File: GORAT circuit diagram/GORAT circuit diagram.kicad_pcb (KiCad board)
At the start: 2 copper layers, 56 x 56 mm, 51 parts, among them J1 AudioJack2, J2 AudioJack2, J3 Barrel_Jack_PTH_Slot, J4 Conn_01x09_Socket, J5 Conn_01x09_Socket, SW3 SW_Rotary4x3, U1 LM308N

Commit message: asdsa
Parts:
- added C18: 470n, Capacitor_THT:C_Disc_D4.7mm_W2.5mm_P5.00mm, F.Cu at (47.6, 49.1)
- added C19: 1u, Capacitor_THT:CP_Radial_D5.0mm_P2.50mm, F.Cu at (56.3, 50.4)
- added R15: 22k, Resistor_THT:R_Axial_DIN0207_L6.3mm_D2.5mm_P10.16mm_Horizontal, F.Cu at (70.8, 37.4)
- added R16: 22k, Resistor_THT:R_Axial_DIN0207_L6.3mm_D2.5mm_P10.16mm_Horizontal, F.Cu at (70.8, 41.4)
- added R17: 22k, Resistor_THT:R_Axial_DIN0207_L6.3mm_D2.5mm_P10.16mm_Horizontal, F.Cu at (70.8, 45.5)
- added R18: 1M, Resistor_THT:R_Axial_DIN0207_L6.3mm_D2.5mm_P10.16mm_Horizontal, F.Cu at (70.8, 49.5)
- added RV4-BLEND1: 100K, Connector_Wire:SolderWire-0.75sqmm_1x06_P7mm_D1.25mm_OD3.5mm, F.Cu at (179.5, 88.0)
- added U2: TL072ACP, PCM_Package_DIP_AKL:DIP-8_W7.62mm_LongPads, F.Cu at (48.0, 37.4)
- added U3: TL072ACP, PCM_Package_DIP_AKL:DIP-8_W7.62mm_LongPads, F.Cu at (59.6, 37.4)
- moved R13 64.6 mm to (178.0, 112.5), turned to 180 degrees
- moved D4 58.9 mm to (177.0, 124.0)
- moved J5 56.8 mm to (158.8, 108.0)
- moved S1 56.6 mm to (163.5, 124.0)
- moved J2 51.7 mm to (122.0, 54.0)
- moved J1 51.6 mm to (163.5, 53.5)
- moved SW3 49.6 mm to (121.4, 116.4)
- moved RV2-FILTER1 46.8 mm to (127.5, 71.5)
- moved RV1-GAIN1 44.5 mm to (113.0, 78.0)
- moved RV3-VOL1 38.3 mm to (147.5, 71.5)
- moved J4 27.1 mm to (156.8, 92.5)
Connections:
- C1 pad 2: Net-(C1-Pad2) -> Net-(U2A-+)
- R2 pad 1: Net-(C1-Pad2) -> Net-(U2A-+)
- R3 pad 2: Net-(C1-Pad2) -> Net-(U2A--)
- RV3-VOL1 pad 2: SigOut -> SigRAT
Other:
- board outline removed

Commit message: almost done
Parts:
- added J6: Barrel_Jack, Connector_Wire:SolderWire-0.5sqmm_1x02_P4.6mm_D0.9mm_OD2.1mm, F.Cu at (73.0, 69.0)
- added J7: Conn_01x02_Socket, Connector_PinHeader_2.54mm:PinHeader_1x02_P2.54mm_Vertical, F.Cu at (25.3, 90.5)
- added J8: Conn_01x03_Socket, Connector_PinHeader_2.54mm:PinHeader_1x03_P2.54mm_Vertical, F.Cu at (59.8, 97.0)
- added J9: Conn_01x03_Socket, Connector_PinHeader_2.54mm:PinHeader_1x03_P2.54mm_Vertical, F.Cu at (59.8, 90.5)
- added SW8: SW_Rotary2x6, Daves customs:RS26, F.Cu at (62.5, 120.2)
- J3: value Barrel_Jack_PTH_Slot -> Conn_01x08_Socket; footprint PCM_SparkFun-Connector:Barrel_Jack_PTH_Slot -> Connector_PinHeader_2.54mm:PinHeader_1x08_P2.54mm_Vertical
- J4: value Conn_01x09_Socket -> Conn_01x08_Socket; footprint Connector_PinHeader_2.54mm:PinHeader_1x09_P2.54mm_Vertical -> Connector_PinHeader_2.54mm:PinHeader_1x08_P2.54mm_Vertical
- J5: value Conn_01x09_Socket -> Conn_01x02_Socket; footprint Connector_PinHeader_2.54mm:PinHeader_1x09_P2.54mm_Vertical -> Connector_PinHeader_2.54mm:PinHeader_1x02_P2.54mm_Vertical
- RV1-GAIN1, RV2-FILTER1, RV3-VOL1: footprint Connector_Wire:SolderWire-0.75sqmm_1x03_P7mm_D1.25mm_OD3.5mm -> Daves customs:Potentiometer_Alpha_RD901F-40-00D_Single_Vertical
- RV4-BLEND1: footprint Connector_Wire:SolderWire-0.75sqmm_1x06_P7mm_D1.25mm_OD3.5mm -> Potentiometer_THT:Potentiometer_Alpha_RD902F-40-00D_Dual_Vertical
- SW3: footprint Daves customs:Rotary Switch -> Daves customs:RS26
- moved J5 133.9 mm to (25.3, 97.0)
- moved C5 96.0 mm to (29.7, 103.5)
- moved R1 93.3 mm to (108.5, 83.0), turned to 180 degrees
- moved R13 92.8 mm to (85.5, 120.1), turned to 90 degrees
- moved D4 91.3 mm to (85.8, 126.0), turned to 180 degrees
- moved RV1-GAIN1 87.7 mm to (25.3, 78.0), turned to 90 degrees
- moved SW3 86.2 mm to (35.3, 120.2), turned to 75 degrees
- moved R15 83.1 mm to (127.3, 98.3), turned to 180 degrees
- moved U3 81.4 mm to (113.6, 98.3), turned to 180 degrees
- moved R12 79.6 mm to (96.3, 121.1), turned to 90 degrees
- moved C6 79.3 mm to (48.1, 103.5)
- moved J2 78.9 mm to (47.0, 78.5)
- moved R16 77.4 mm to (127.3, 94.3), turned to 180 degrees
- moved R2 76.3 mm to (88.0, 85.9), turned to -90 degrees
- moved R11 72.8 mm to (96.9, 102.5), turned to 180 degrees
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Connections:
- C14 pad 2: GND -> GND3
- C15 pad 2: GND -> GND3
- C16 pad 2: GND -> GND3
- C17 pad 2: GND -> GND3
- C4 pad 2: Net-(U1--) -> Net-(J7-Pin_1)
- C5 pad 2: GND -> GND3
- C6 pad 2: GND -> GND3
- D1 pad 2: GND -> GND3
- D2 pad 1: GND -> GND3
- D4 pad 2: Vin -> Vin1
- D5 pad 2: GND -> GND3
- D6 pad 1: Net-(D6-K) -> GND3
- D6 pad 2: GND -> Net-(D6-A)
- D7 pad 2: GND -> GND3
- D8 pad 1: Net-(D8-K) -> GND3
- D8 pad 2: GND -> Net-(D8-A)
- J1 pad 1: /JackIn -> /JackIn1
- J2 pad 1: /JackOut -> /JackOut1
- J4 pad 1: Bypass -> Bypass2
- J4 pad 2: /JackIn -> /JackIn2
- J4 pad 3: /JackOut -> /JackOut2
- J4 pad 4: SigIn -> SigIn2
- J4 pad 5: SigOut -> SigOut2
- J4 pad 6: /+9v Jack -> /+9v Jack2
- J4 pad 7: Vin -> Vin2
- J4 pad 8: GND -> GND2
- J5 pad 1: Bypass -> Net-(J5-Pin_1)
- J5 pad 2: /JackIn -> GND3
- R1 pad 2: /JackIn -> /JackIn1
- R10 pad 1: Vin -> Vin1
- R14 pad 2: /JackOut -> /JackOut1
- R4 pad 1: Net-(U1--) -> Net-(J5-Pin_1)
- R5 pad 1: Net-(U1--) -> Net-(J5-Pin_1)
- R6 pad 1: Net-(R6-Pad1) -> Net-(J9-Pin_1)
- RV1-GAIN1 pad 1: Net-(U1--) -> Net-(J7-Pin_1)
- RV1-GAIN1 pad 2: Net-(U1--) -> Net-(J7-Pin_1)
- RV2-FILTER1 pad 1: Net-(R6-Pad1) -> Net-(J9-Pin_1)
- RV2-FILTER1 pad 2: Net-(R6-Pad1) -> Net-(R7-Pad2)
- RV3-VOL1 pad 1: Net-(C10-Pad2) -> GND
- RV3-VOL1 pad 3: GND -> Net-(C10-Pad2)
- RV4-BLEND1 pad 5: SigDRY -> Net-(R17-Pad1)
- S1 pad P$1: SigOut -> SigOut2
- S1 pad P$2: /JackOut -> /JackOut2
- S1 pad P$3: Bypass -> Net-(S1A-S)
- S1 pad P$4: SigIn -> SigIn2
- S1 pad P$5: /JackIn -> /JackIn2
- S1 pad P$6: Bypass -> Net-(S1A-S)
- S1 pad P$7: /+9v Jack -> /+9v Jack2
- S1 pad P$8: Vin -> Vin2
- U1 pad 2: Net-(U1--) -> Net-(J7-Pin_1)
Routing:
- net GND: track 0.00 -> 217.3 mm
- net +9V: track 0.00 -> 113.1 mm
- net GND3: track 0.00 -> 111.3 mm
- net /JackOut1: track 0.00 -> 92.3 mm, vias 0 -> 1
- net /+9v Jack1: track 0.00 -> 77.1 mm, vias 0 -> 1
- net Net-(J7-Pin_1): track 0.00 -> 72.9 mm
- net Net-(C4-Pad1): track 0.00 -> 60.9 mm
- net +4.5V: track 0.00 -> 58.9 mm
- net Vin1: track 0.00 -> 53.4 mm
- net Net-(D7-K): track 0.00 -> 50.4 mm
- net Net-(C9-Pad1): track 0.00 -> 45.5 mm, vias 0 -> 1
- net /JackIn1: track 0.00 -> 43.3 mm
- net Net-(R4-Pad2): track 0.00 -> 42.5 mm, vias 0 -> 1
- net Net-(J9-Pin_1): track 0.00 -> 41.1 mm
- net SigRAT: track 0.00 -> 36.4 mm
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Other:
- board outline added: 107.5 x 71.5 mm

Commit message: close to done
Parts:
- removed JN1: 2N5458, 2N5458:TO92
- added C20: 220n, Capacitor_THT:C_Disc_D5.1mm_W3.2mm_P5.00mm, F.Cu at (35.5, 100.5)
- added C21: 470n, Capacitor_THT:C_Disc_D5.1mm_W3.2mm_P5.00mm, F.Cu at (51.0, 109.5)
- added C22: 33p, Capacitor_THT:C_Disc_D4.7mm_W2.5mm_P5.00mm, F.Cu at (57.5, 106.0)
- added J10: Conn_01x02_Socket, Connector_PinHeader_2.54mm:PinHeader_1x02_P2.54mm_Vertical, F.Cu at (33.2, 90.5)
- added J11: Conn_01x02_Socket, Connector_PinHeader_2.54mm:PinHeader_1x02_P2.54mm_Vertical, F.Cu at (33.5, 97.0)
- added Q1: J111, PCM_Package_TO_SOT_THT_AKL:TO-92_Inline_Wide_DSG, F.Cu at (65.5, 83.6)
- C16: value Xu -> 68p; footprint Capacitor_THT:CP_Radial_D5.0mm_P2.50mm -> Capacitor_THT:C_Disc_D4.7mm_W2.5mm_P5.00mm
- C17: value Xu -> 47p; footprint Capacitor_THT:CP_Radial_D5.0mm_P2.50mm -> Capacitor_THT:C_Disc_D4.7mm_W2.5mm_P5.00mm
- U1: value LM308N -> OP07CP
- moved C16 18.4 mm to (54.0, 106.0), turned to 90 degrees
- moved D1 13.5 mm to (72.5, 108.0)
- moved R5 7.45 mm to (39.3, 96.0)
- moved C17 7.16 mm to (61.0, 106.0), turned to 90 degrees
- moved R4 6.57 mm to (39.4, 99.5)
- moved D8 5.52 mm to (77.5, 112.2)
- moved D2 3.74 mm to (79.8, 105.0)
- moved C6 2.10 mm to (47.5, 105.5), turned to 90 degrees
- moved C15 1.71 mm to (42.0, 105.2), turned to 90 degrees
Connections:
- C16 pad 2: GND3 -> Net-(J11-Pin_2)
- C17 pad 2: GND3 -> Net-(J11-Pin_2)
- SW3 pad 15: unconnected-(SW3-Pad15) -> Net-(J11-Pin_1)
- SW3 pad 3: Net-(C16-Pad1) -> Net-(C20-Pad2)
- SW3 pad 6: Net-(C17-Pad1) -> Net-(C21-Pad2)
- SW3 pad 7: unconnected-(SW3-Pad7) -> Net-(C16-Pad1)
- SW3 pad 8: unconnected-(SW3-Pad8) -> Net-(C17-Pad1)
- SW3 pad 9: unconnected-(SW3-Pad9) -> Net-(C22-Pad1)
- U1 pad 1: Net-(C3-Pad1) -> Net-(J10-Pin_2)
- U1 pad 8: Net-(C3-Pad2) -> Net-(J10-Pin_1)
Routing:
- net Net-(J10-Pin_1): track 0.00 -> 47.4 mm
- net Net-(J10-Pin_2): track 0.00 -> 44.3 mm, vias 0 -> 1
- net Net-(C22-Pad1): track 0.00 -> 34.6 mm
- net Net-(J11-Pin_1): track 0.00 -> 29.6 mm
- net Net-(J11-Pin_2): track 0.00 -> 26.7 mm
- net Net-(C17-Pad1): track 17.2 -> 31.2 mm
- net Net-(C16-Pad1): track 7.33 -> 20.3 mm
- net /+9v Jack1: track 77.1 -> 65.8 mm
- net Net-(R4-Pad2): track 42.5 -> 31.9 mm
- net Net-(C21-Pad2): track 0.00 -> 7.79 mm
- net Net-(D1-K): track 27.7 -> 33.7 mm
- net Net-(C20-Pad2): track 0.00 -> 5.20 mm
- net Net-(D7-K): track 50.4 -> 45.4 mm
- net Net-(J5-Pin_1): track 22.5 -> 18.3 mm
- net Net-(D2-A): track 19.8 -> 16.4 mm
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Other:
- board size 107.5 x 71.5 mm -> 108.5 x 71.5 mm
- board text added: "+9V"
- board text added: "Board 1 : The meat and potatoes"
- board text added: "Board 2 : Tone Selekta"
- board text added: "Board 3 : Stompy"
- board text added: "GND"
- board text added: "Output"

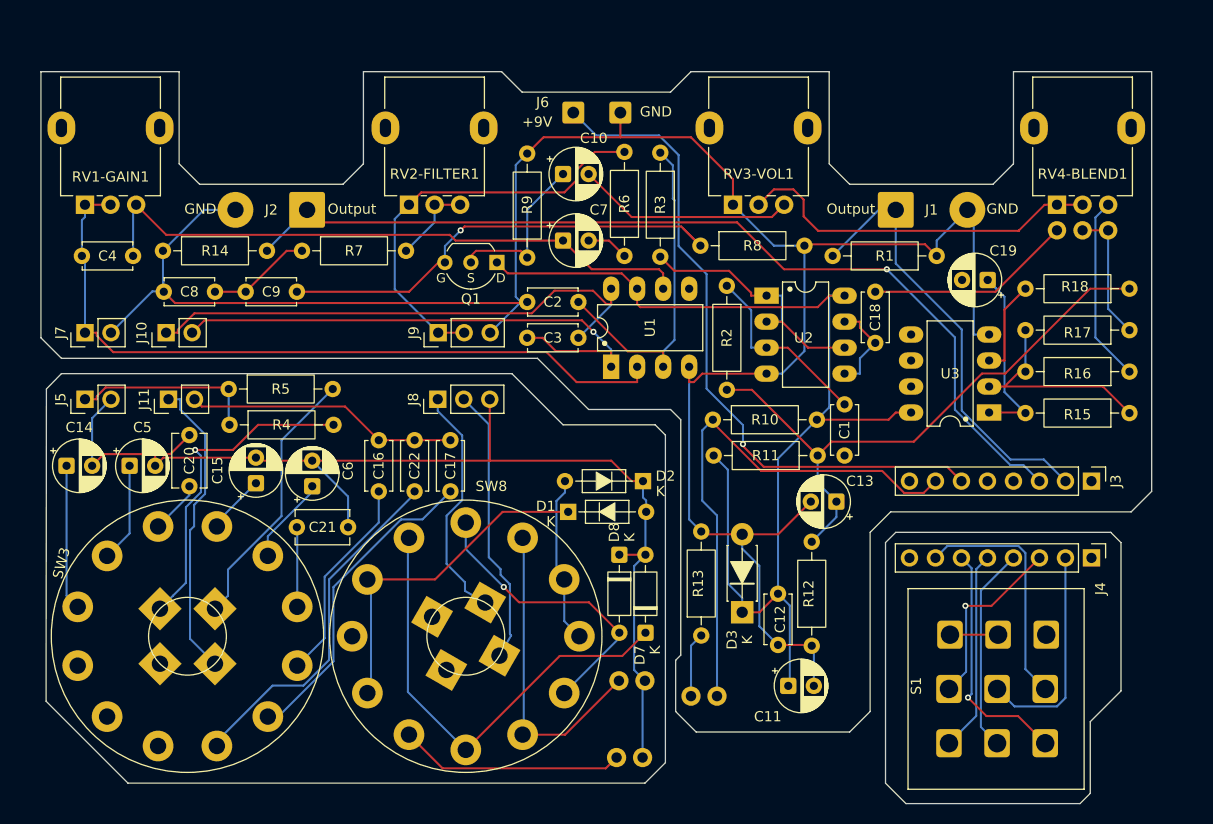
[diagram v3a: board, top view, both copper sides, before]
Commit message: Update KiCad PCB, add backups and artwork
Modify GORAT circuit diagram.kicad_pcb: reorder/renumber nets, adjust several pad/net assignments and component positions, and add numerous F.Fab properties (Availability, Check_prices, Description_1, MF, MP, Package, Price, Sim.Type, SnapEDA_Link) for multiple footprints. Remove several old backup ZIPs and add new timestamped backup ZIPs. Add new project assets: GoRAT.csv and artwork/renders (goram-mirror.svg, goram.png, goram.svg, underside.svg). These changes appear to be from a PCB/footprint update and exporting backup/artwork files.
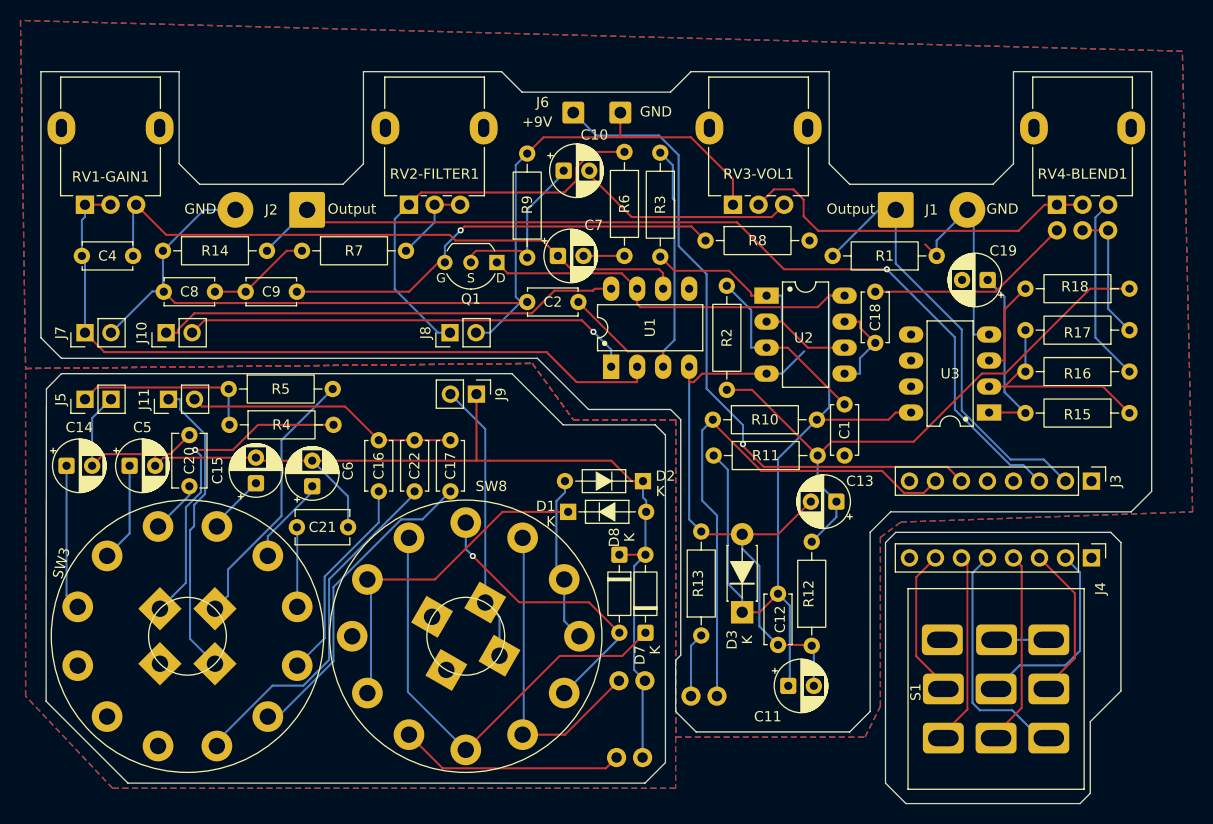
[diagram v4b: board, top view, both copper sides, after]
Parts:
- removed C3: 30p, Capacitor_THT:C_Disc_D4.7mm_W2.5mm_P5.00mm
- J8, J9: value Conn_01x03_Socket -> Conn_01x02_Socket; footprint Connector_PinHeader_2.54mm:PinHeader_1x03_P2.54mm_Vertical -> Connector_PinHeader_2.54mm:PinHeader_1x02_P2.54mm_Vertical
- moved J9 7.07 mm to (63.5, 96.5), turned to -90 degrees
- moved J8 6.61 mm to (61.0, 90.5)
- moved C7 1.58 mm to (71.5, 83.0)
- moved R8 0.71 mm to (85.9, 81.5)
- moved C10 0.33 mm to (72.1, 74.7)
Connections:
- net Net-(S1A-S) renamed /Bypass
- J8 pad 2: Net-(J8-Pin_2) -> GND
- J9 pad 1: Net-(J9-Pin_1) -> GND3
- J9 pad 2: Net-(J9-Pin_1) -> Net-(J9-Pin_2)
- R6 pad 1: Net-(J9-Pin_1) -> Net-(J8-Pin_1)
- RV2-FILTER1 pad 1: Net-(J9-Pin_1) -> Net-(J8-Pin_1)
- SW8 pad 13: Net-(J8-Pin_1) -> Net-(J9-Pin_2)
- SW8 pad 14: Net-(J8-Pin_2) -> Net-(J9-Pin_2)
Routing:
- net Net-(J9-Pin_1): track 41.1 -> 0.00 mm
- net GND: track 218.6 -> 189.4 mm
- net Net-(J9-Pin_2): track 0.00 -> 27.5 mm
- net Net-(J8-Pin_2): track 27.3 -> 0.00 mm
- net Net-(J8-Pin_1): track 23.4 -> 39.9 mm
- net Net-(C3-Pad1): track 10.2 -> 0.00 mm
- net Vin2: track 23.6 -> 14.2 mm
- net Net-(C3-Pad2): track 6.12 -> 0.00 mm
- net /+9v Jack2: track 23.6 -> 18.3 mm, vias 1 -> 0
- net SigOut2: track 19.7 -> 23.5 mm
- net /JackOut2: track 18.0 -> 14.8 mm, vias 1 -> 0
- net Net-(Q1-G): track 46.1 -> 44.1 mm
- net /JackIn2: track 21.4 -> 19.4 mm
- net Net-(J10-Pin_1): track 47.4 -> 45.4 mm
- net SigIn2: track 20.1 -> 18.4 mm
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- added copper zone on B.Cu, net GND
- added copper zone on F.Cu, net GND
- added copper zone on B.Cu, net GND3
- added copper zone on F.Cu, net GND3
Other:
- board text added: "GoRAT Distortion Effect V1.1 RandomAccessCrew"

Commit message: Update disc capacitor footprints and BOM
Replace THT disc capacitor footprints with smaller C_Disc_D4.7mm_W2.5mm variants across schematic and PCB (updated 3D model paths, silk/text positions, rotations and UUIDs). Update project metadata: change active board layer in .kicad_prl, set BOM export filename in .kicad_pro, and add generated BOM CSV/XLSX. Add KiCad backup archives and remove autosave/.lck temporary files to keep the repo clean.
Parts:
- C20, C21: footprint Capacitor_THT:C_Disc_D5.1mm_W3.2mm_P5.00mm -> Capacitor_THT:C_Disc_D4.7mm_W2.5mm_P5.00mm
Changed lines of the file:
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@@
 		)
 	)
-	(footprint "Capacitor_THT:C_Disc_D5.1mm_W3.2mm_P5.00mm"
+	(footprint "Capacitor_THT:C_Disc_D4.7mm_W2.5mm_P5.00mm"
 		(layer "F.Cu")
 		(at 51 109.5 180)
-		(descr "C, Disc series, Radial, pin pitch=5.00mm, diameter*width=5.1*3.2mm^2, Capacitor, http://www.vishay.com/docs/45233/krseries.pdf")
-		(tags "C Disc series Radial pin pitch 5.00mm diameter 5.1mm width 3.2mm Capacitor")
+		(descr "C, Disc series, Radial, pin pitch=5.00mm, diameter*width=4.7*2.5mm^2, Capacitor, http://www.vishay.com/docs/45233/krseries.pdf")
+		(tags "C Disc series Radial pin pitch 5.00mm diameter 4.7mm width 2.5mm Capacitor")
 		(property "Reference" "C21"
-			(at 2.5 0 0)
+			(at 2.5 -2.5 180)
 			(layer "F.SilkS")
 			(effects
@@
 		)
 		(property "Value" "470n"
-			(at 2.5 2.85 0)
+			(at 2.5 2.5 180)
 			(layer "F.Fab")
 			(effects
@@
 		)
 		(property "Datasheet" "~"
-			(at 0 0 0)
+			(at 0 0 180)
 			(layer "F.Fab")
 			(hide yes)
@@
 		)
 		(property "Description" "Unpolarized capacitor"
-			(at 0 0 0)
+			(at 0 0 180)
 			(layer "F.Fab")
 			(hide yes)
@@
 		(attr through_hole)
 		(fp_line
-			(start 5.17 1.72)
-			(end -0.17 1.72)
+			(start 4.97 1.37)
+			(end 0.03 1.37)
 			(stroke
 				(width 0.12)
@@
 		)
 		(fp_line
-			(start 5.17 1.026)
-			(end 5.17 1.72)
+			(start 4.97 1.04)
+			(end 4.97 1.37)
 			(stroke
 				(width 0.12)
@@
 		)
 		(fp_line
-			(start 5.17 -1.72)
-			(end 5.17 -1.026)
+			(start 4.97 -1.37)
+			(end 4.97 -1.04)
 			(stroke
 				(width 0.12)
@@
 		)
 		(fp_line
-			(start -0.17 1.72)
-			(end -0.17 1.026)
+			(start 0.03 1.37)
+			(end 0.03 1.04)
 			(stroke
 				(width 0.12)
@@
 		)
 		(fp_line
-			(start -0.17 -1.026)
-			(end -0.17 -1.72)
+			(start 0.03 -1.04)
+			(end 0.03 -1.37)
 			(stroke
 				(width 0.12)
@@
 		)
 		(fp_line
-			(start -0.17 -1.72)
-			(end 5.17 -1.72)
+			(start 0.03 -1.37)
+			(end 4.97 -1.37)
 			(stroke
 				(width 0.12)
@@
 		)
 		(fp_rect
-			(start -1.05 -1.85)
-			(end 6.05 1.85)
+			(start -1.05 -1.5)
+			(end 6.05 1.5)
 			(stroke
 				(width 0.05)
@@
 		)
 		(fp_rect
-			(start -0.05 -1.6)
-			(end 5.05 1.6)
+			(start 0.15 -1.25)
+			(end 4.85 1.25)
 			(stroke
 				(width 0.1)
@@
 		)
 		(fp_text user "${REFERENCE}"
-			(at 2.5 0 0)
+			(at 2.5 0 180)
 			(layer "F.Fab")
 			(effects
 				(font
-					(size 1 1)
-					(thickness 0.15)
+					(size 0.94 0.94)
+					(thickness 0.141)
 				)
 			)
@@
 		)
 		(embedded_fonts no)
-		(model "${KICAD9_3DMODEL_DIR}/Capacitor_THT.3dshapes/C_Disc_D5.1mm_W3.2mm_P5.00mm.step"
+		(model "${KICAD9_3DMODEL_DIR}/Capacitor_THT.3dshapes/C_Disc_D4.7mm_W2.5mm_P5.00mm.step"
 			(offset
 				(xyz 0 0 0)
@@
 		)
 	)
-	(footprint "Capacitor_THT:C_Disc_D5.1mm_W3.2mm_P5.00mm"
+	(footprint "Capacitor_THT:C_Disc_D4.7mm_W2.5mm_P5.00mm"
 		(layer "F.Cu")
 		(at 35.5 100.5 -90)
-		(descr "C, Disc series, Radial, pin pitch=5.00mm, diameter*width=5.1*3.2mm^2, Capacitor, http://www.vishay.com/docs/45233/krseries.pdf")
-		(tags "C Disc series Radial pin pitch 5.00mm diameter 5.1mm width 3.2mm Capacitor")
+		(descr "C, Disc series, Radial, pin pitch=5.00mm, diameter*width=4.7*2.5mm^2, Capacitor, http://www.vishay.com/docs/45233/krseries.pdf")
+		(tags "C Disc series Radial pin pitch 5.00mm diameter 4.7mm width 2.5mm Capacitor")
 		(property "Reference" "C20"
-			(at 2.5 0 90)
+			(at 2.5 0 270)
 			(layer "F.SilkS")
 			(effects
@@
 		)
 		(property "Value" "220n"
-			(at 2.5 2.85 90)
+			(at 2.5 2.5 270)
 			(layer "F.Fab")
 			(effects
@@
 		)
 		(property "Datasheet" "~"
-			(at 0 0 90)
+			(at 0 0 270)
 			(layer "F.Fab")
 			(hide yes)
@@
 		)
 		(property "Description" "Unpolarized capacitor"
-			(at 0 0 90)
+			(at 0 0 270)
 			(layer "F.Fab")
 			(hide yes)
@@
 		(attr through_hole)
 		(fp_line
-			(start -0.17 1.72)
-			(end -0.17 1.026)
+			(start 0.03 1.37)
+			(end 0.03 1.04)
 			(stroke
 				(width 0.12)
@@
 		)
 		(fp_line
-			(start 5.17 1.72)
-			(end -0.17 1.72)
+			(start 4.97 1.37)
+			(end 0.03 1.37)
 			(stroke
 				(width 0.12)
@@
 		)
 		(fp_line
-			(start 5.17 1.026)
-			(end 5.17 1.72)
+			(start 4.97 1.04)
+			(end 4.97 1.37)
 			(stroke
 				(width 0.12)
@@
 		)
 		(fp_line
-			(start -0.17 -1.026)
-			(end -0.17 -1.72)
+			(start 0.03 -1.04)
+			(end 0.03 -1.37)
 			(stroke
 				(width 0.12)
@@
 		)
 		(fp_line
-			(start -0.17 -1.72)
-			(end 5.17 -1.72)
+			(start 0.03 -1.37)
+			(end 4.97 -1.37)
 			(stroke
 				(width 0.12)
@@
 		)
 		(fp_line
-			(start 5.17 -1.72)
-			(end 5.17 -1.026)
+			(start 4.97 -1.37)
+			(end 4.97 -1.04)
 			(stroke
 				(width 0.12)
@@
 		)
 		(fp_rect
-			(start -1.05 -1.85)
-			(end 6.05 1.85)
+			(start -1.05 -1.5)
+			(end 6.05 1.5)
 			(stroke
 				(width 0.05)
@@
 		)
 		(fp_rect
-			(start -0.05 -1.6)
-			(end 5.05 1.6)
+			(start 0.15 -1.25)
+			(end 4.85 1.25)
 			(stroke
 				(width 0.1)
@@
 		)
 		(fp_text user "${REFERENCE}"
-			(at 2.5 0 90)
+			(at 2.5 0 270)
 			(layer "F.Fab")
 			(effects
 				(font
-					(size 1 1)
-					(thickness 0.15)
+					(size 0.94 0.94)
+					(thickness 0.141)
 				)
 			)
@@
 		)
 		(embedded_fonts no)
-		(model "${KICAD9_3DMODEL_DIR}/Capacitor_THT.3dshapes/C_Disc_D5.1mm_W3.2mm_P5.00mm.step"
+		(model "${KICAD9_3DMODEL_DIR}/Capacitor_THT.3dshapes/C_Disc_D4.7mm_W2.5mm_P5.00mm.step"
 			(offset
 				(xyz 0 0 0)
